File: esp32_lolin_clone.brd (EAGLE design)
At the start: 25 x 58 mm, 33 parts, among them J1 10104111-0001LF, P1 S2B-PH-SM4-TB, Q1 CJ2301S1, Q2 CJ2301S1, SW1 PTS815SJK250SMTR, U1 ESP32-WROOM-32D, U2 BCM857, U3 ME6211, U4 UMH3N, U5 TP4054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

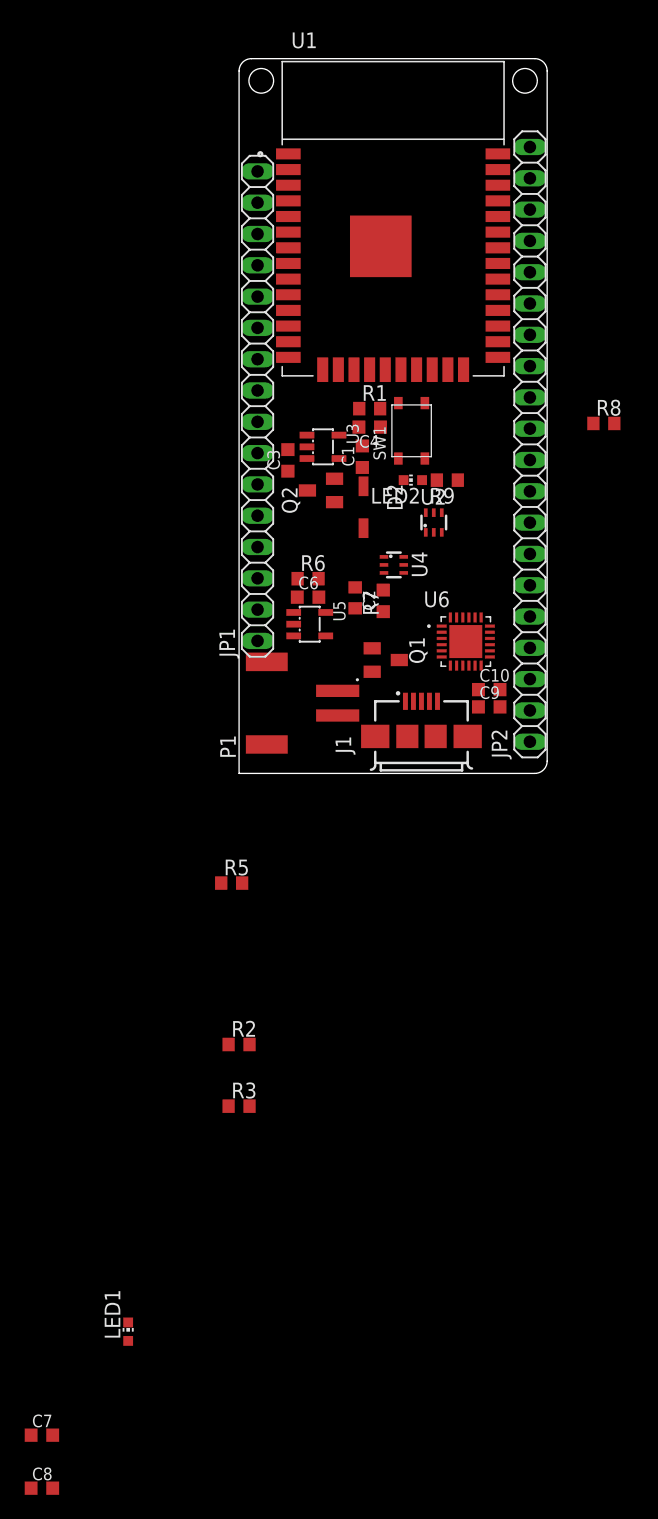
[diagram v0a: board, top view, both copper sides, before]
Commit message: Routing and changing position of some components.
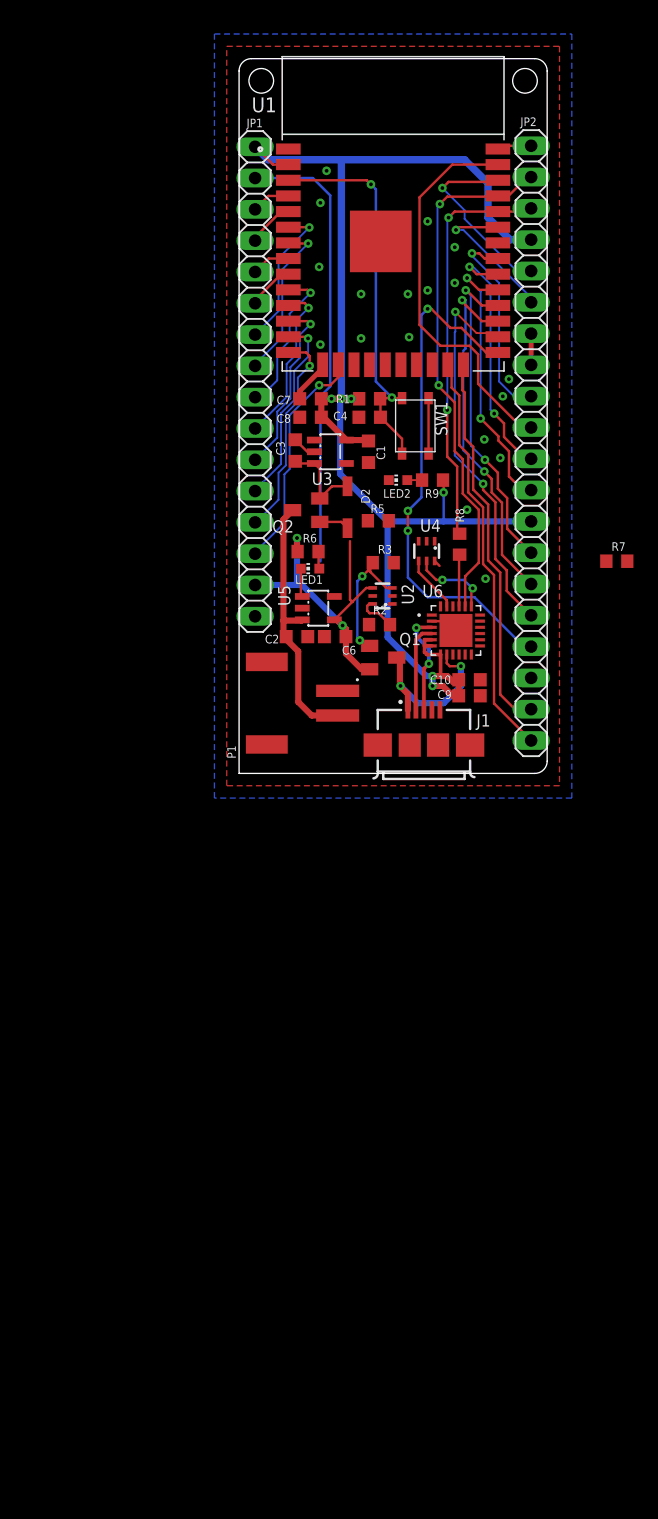
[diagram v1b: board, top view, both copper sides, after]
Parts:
- moved C8 89.6 mm to (5.80, 28.9), turned to 180 degrees
- moved C7 86.9 mm to (5.80, 30.4), turned to 180 degrees
- moved LED1 63.7 mm to (5.76, 16.6), turned to 90 degrees
- moved R3 45.6 mm to (11.7, 17.1)
- moved R2 35.9 mm to (11.4, 12.1)
- moved R5 31.7 mm to (11.3, 20.5)
- moved R7 21.4 mm to (30.7, 17.2), turned to 0 degrees
- moved R8 15.3 mm to (17.9, 18.6), turned to 90 degrees
- moved C2 7.58 mm to (4.70, 11.1), turned to 0 degrees
- moved U2 7.27 mm to (11.6, 14.4), turned to 90 degrees
- moved C6 3.88 mm to (7.80, 11.1), turned to 180 degrees
- moved U4 2.89 mm to (15.2, 18.0), turned to 180 degrees
- moved R6 2.20 mm to (5.60, 18.0)
- moved JP1 2.01 mm to (1.30, 31.8), turned to 270 degrees
- moved Q2 2.00 mm to (5.45, 21.4)
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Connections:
- net N$11 renamed ESP32_EN
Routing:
- net +3V3: track 0.00 -> 114.1 mm, vias 0 -> 6
- net TXD0: track 0.00 -> 42.9 mm, vias 0 -> 2
- net IO0: track 0.00 -> 42.0 mm, vias 0 -> 3
- net EN: track 0.00 -> 37.3 mm
- net IO15: track 0.00 -> 33.3 mm
- net RXD0: track 0.00 -> 33.2 mm, vias 0 -> 2
- net ESP32_EN: track 0.00 -> 31.9 mm, vias 0 -> 2
- net IO23: track 0.00 -> 31.7 mm
- net IO4: track 0.00 -> 31.5 mm, vias 0 -> 2
- net IO2: track 0.00 -> 31.1 mm
- net IO16: track 0.00 -> 29.3 mm, vias 0 -> 2
- net +5V: track 0.00 -> 28.3 mm, vias 0 -> 2
- net IO17: track 0.00 -> 26.6 mm, vias 0 -> 2
- net VBAT: track 0.00 -> 22.7 mm
- net IO5: track 0.00 -> 22.7 mm, vias 0 -> 2
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- added copper zone on layer 1, net GND
- added copper zone on layer 16, net GND

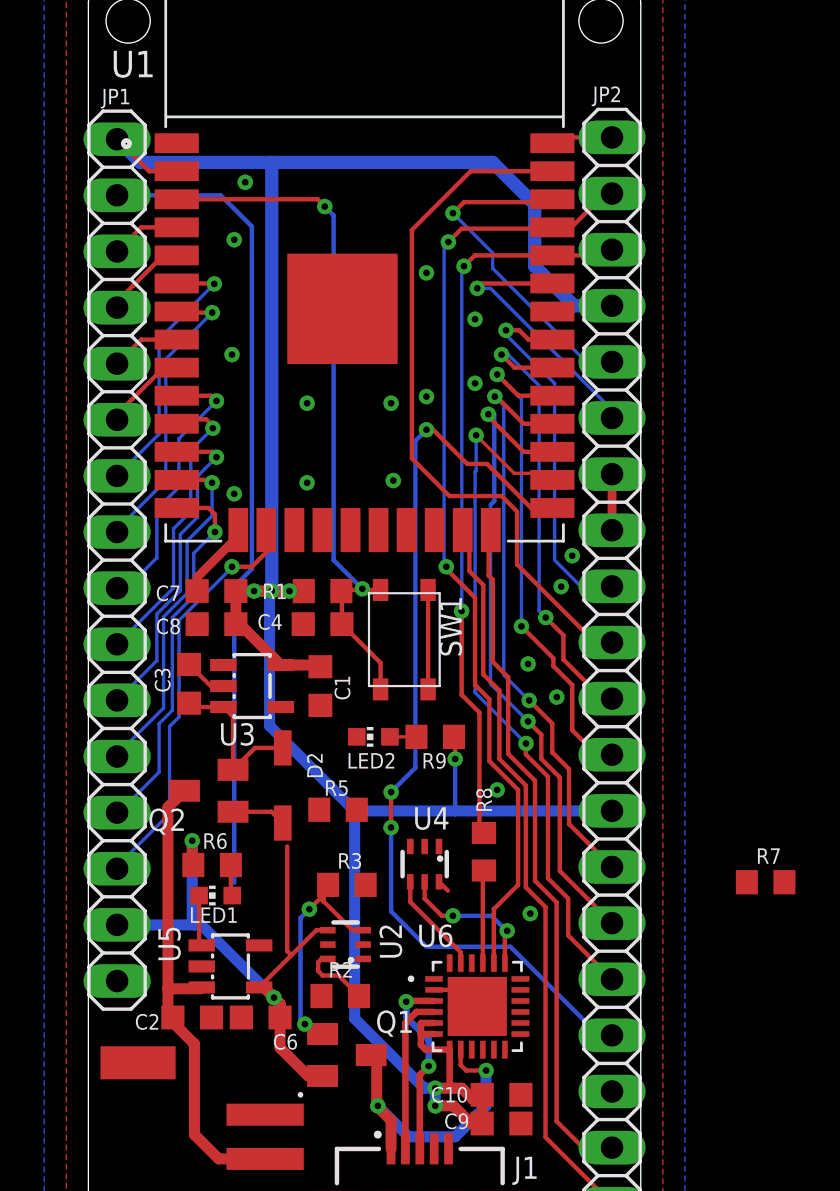
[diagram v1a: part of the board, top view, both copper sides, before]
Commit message: - Finish first routing attempt. - Add notes to schematic.
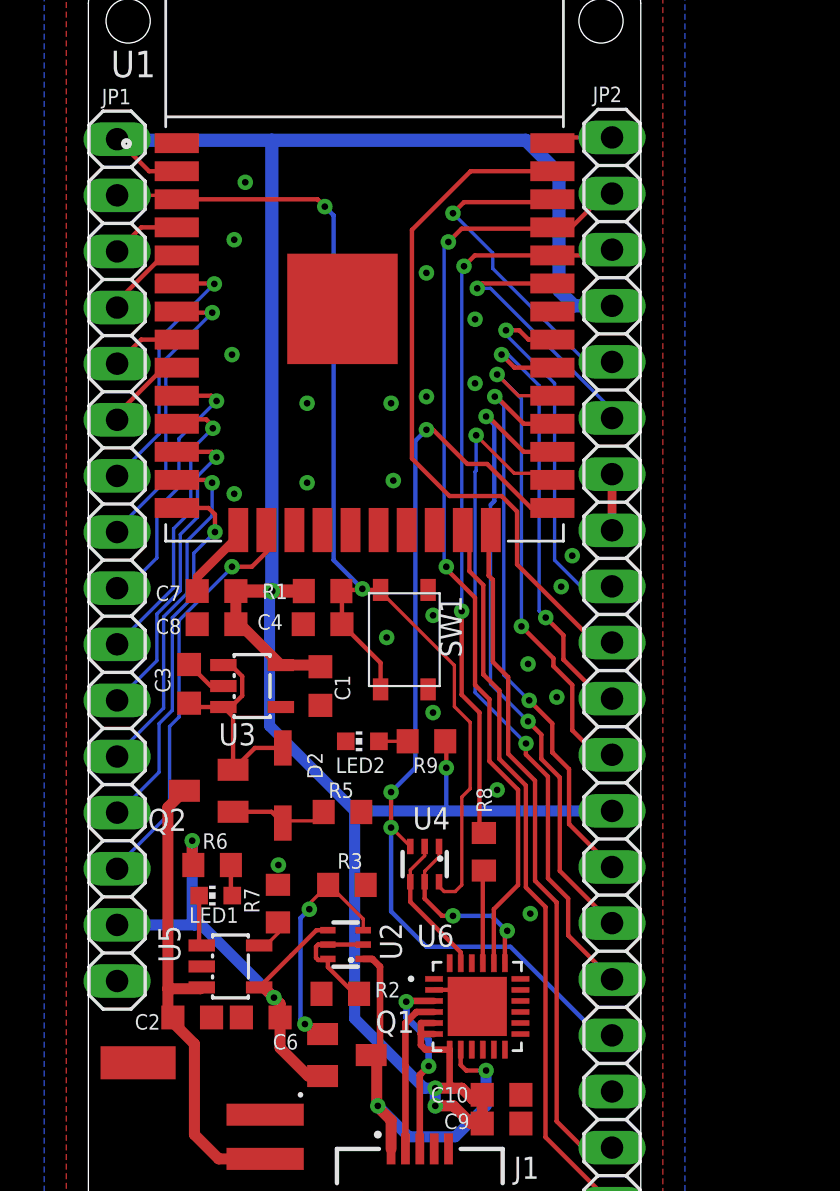
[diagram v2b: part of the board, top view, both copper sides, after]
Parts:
- moved R7 22.1 mm to (8.58, 16.3), turned to 90 degrees
- moved LED2 0.54 mm to (12.4, 23.6)
- moved R9 0.45 mm to (15.3, 23.6)
- moved R5 0.22 mm to (11.5, 20.4)
- moved R2 0.10 mm to (11.4, 12.2)
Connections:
- removed net ESP32_EN: C4.1, R1.2, SW1.1, SW1.2, U1.3
- net EN: now also C4.1, R1.2, SW1.1, SW1.2, U1.3
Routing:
- net ESP32_EN: track 31.9 -> 0.00 mm, vias 2 -> 0
- net EN: track 37.3 -> 51.4 mm, vias 0 -> 2
- net VBUS: track 14.2 -> 19.3 mm
- net +5V: track 28.3 -> 23.3 mm
- net GND: track 17.9 -> 13.4 mm, vias 18 -> 22
- net VIN: track 7.31 -> 10.2 mm
- net N$7: track 3.22 -> 5.68 mm
- net N$5: track 2.46 -> 4.58 mm
- net DTR: track 4.63 -> 6.50 mm
- net RTS: track 6.82 -> 8.69 mm
- net IO0: track 42.0 -> 43.2 mm
- net N$14: track 0.45 -> 1.57 mm
- net +3V3: track 114.1 -> 114.9 mm, vias 6 -> 4

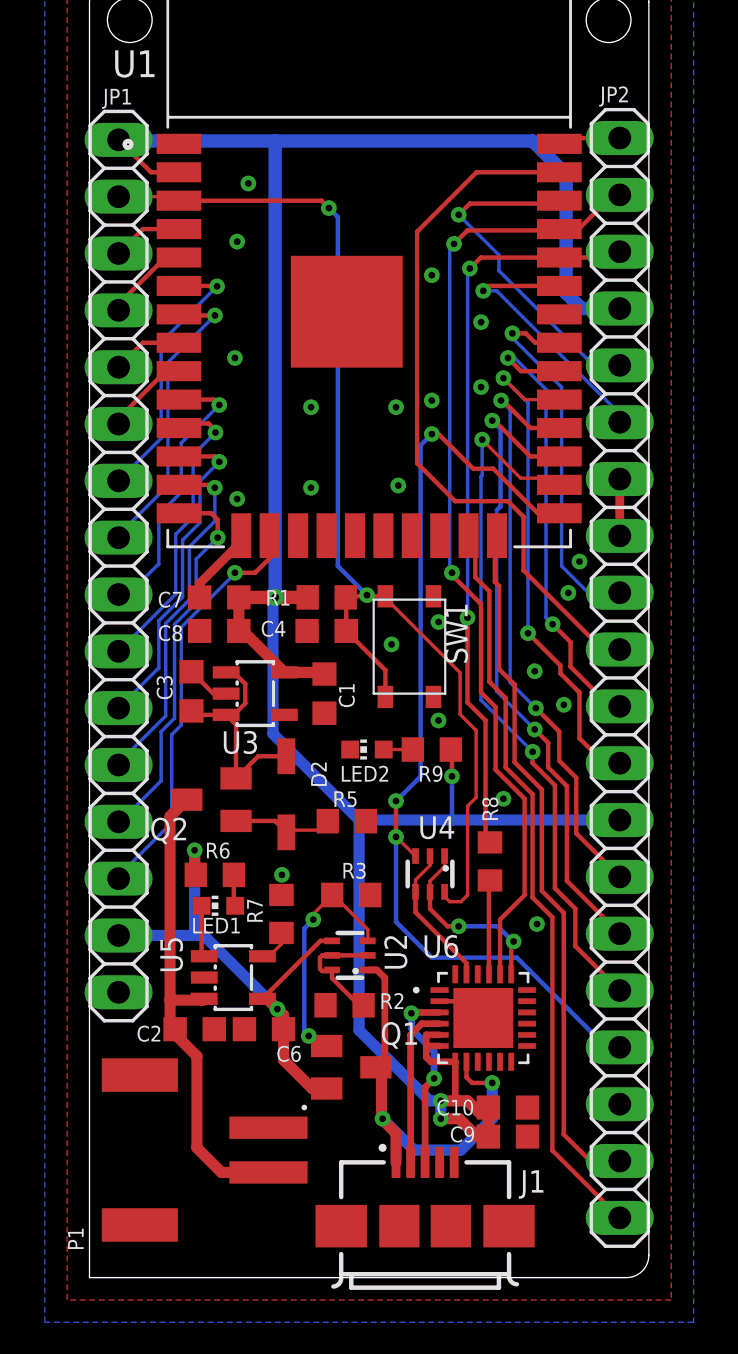
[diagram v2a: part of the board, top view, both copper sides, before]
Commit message: - set traces to the correct size.
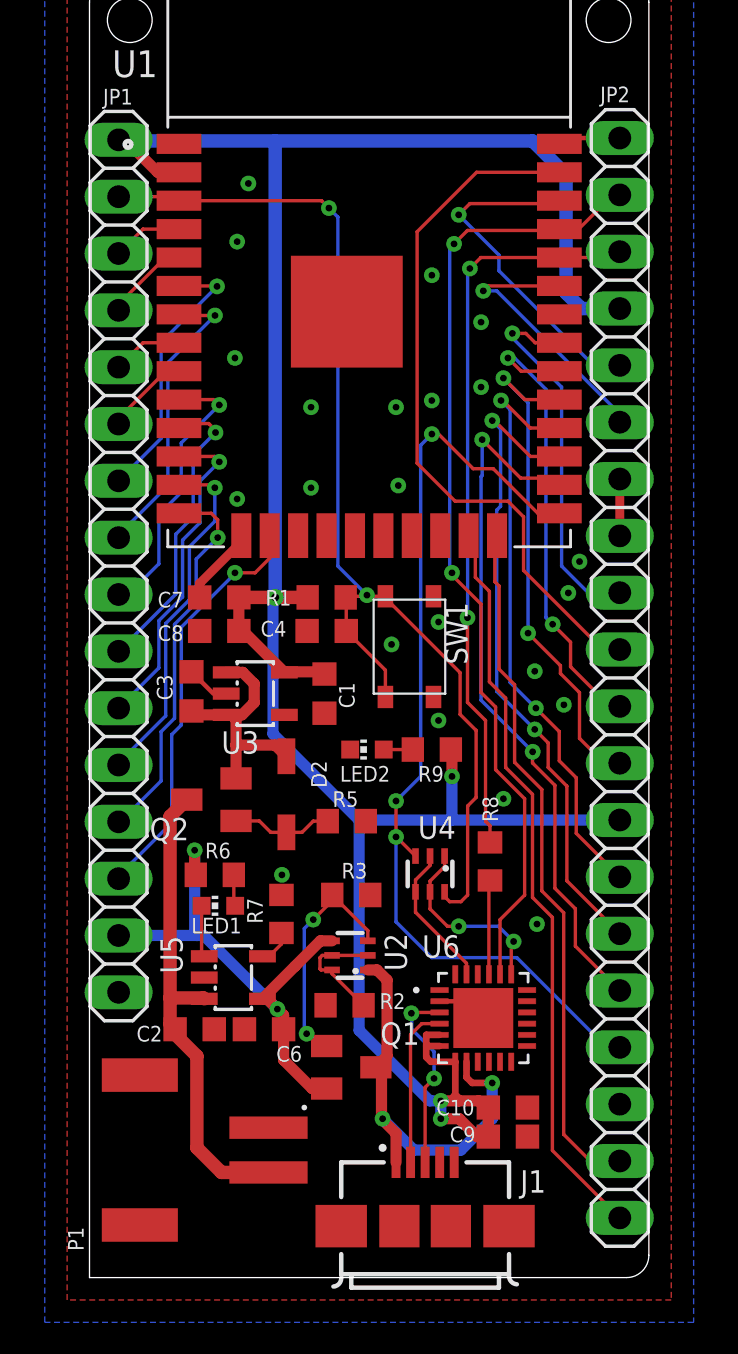
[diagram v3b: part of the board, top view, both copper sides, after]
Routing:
- net VBAT: track 22.7 -> 21.6 mm
- net VIN: track 10.2 -> 11.0 mm
- net N$5: track 4.58 -> 5.09 mm
